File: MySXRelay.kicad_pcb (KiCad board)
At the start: 2 copper layers, 47.2 x 45.1 mm, 53 parts, among them K1 FH44L-1AT-L1-DC5V, Q1 2N7002, U1 MIC4427, U2 BL0942, U3 BP2525X, U4 Si8642BB-B-IS1, U5 MCP1703Ax-180xxTT

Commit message: update schematic to new version
- include MCU, remove MySXMotherboard
- only RS485 interface is isolated
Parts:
- removed X4: ~, Connector_PinSocket_2.54mm:PinSocket_1x04_P2.54mm_Vertical
- removed X5: ~, MySXRelay:JST-XH_S_4P-2.54MM-PIN1-RIGHT
- added C15: 100n, Capacitor_SMD:C_0402_1005Metric, F.Cu at (201.2, 95.6)
- added C16: 100n, Capacitor_SMD:C_0402_1005Metric, F.Cu at (201.2, 97.6)
- added C17: 100n, Capacitor_SMD:C_0402_1005Metric, F.Cu at (201.2, 99.5)
- added C18: 1u/50V, Capacitor_SMD:C_0603_1608Metric, F.Cu at (215.2, 102.4)
- added C19: 10u, Capacitor_SMD:C_0603_1608Metric, F.Cu at (215.2, 104.9)
- added D10: SMAJ11CA, Diode_SMD:D_SMA, F.Cu at (209.2, 101.4)
- added D8: LED, LED_SMD:LED_0805_2012Metric_Pad1.15x1.40mm_HandSolder, F.Cu at (185.9, 114.3)
- added D9: SMAJ11CA, Diode_SMD:D_SMA, F.Cu at (209.2, 96.9)
- added F1: Polyfuse, Fuse:Fuse_1206_3216Metric_Pad1.42x1.75mm_HandSolder, F.Cu at (208.1, 105.3)
- added F2: Polyfuse, Fuse:Fuse_1206_3216Metric_Pad1.42x1.75mm_HandSolder, F.Cu at (208.1, 108.6)
- added J1: AVR ISP, Connector_PinHeader_2.54mm:PinHeader_2x03_P2.54mm_Vertical, F.Cu at (194.3, 108.6)
- added J2: PRG/BL0942, Connector_PinHeader_2.54mm:PinHeader_1x02_P2.54mm_Vertical, F.Cu at (197.5, 96.9)
- added Q2: ~, Package_TO_SOT_SMD:SOT-23, F.Cu at (219.7, 108.2)
- added R19: 1k, Resistor_SMD:R_0603_1608Metric, F.Cu at (201.1, 107.5)
- added R20: 1M, Resistor_SMD:R_0603_1608Metric, F.Cu at (201.1, 110.0)
- added R21: 9.1k, Resistor_SMD:R_0603_1608Metric, F.Cu at (215.2, 107.5)
- added R22: 1M, Resistor_SMD:R_0603_1608Metric, F.Cu at (201.1, 112.5)
- added R23: 3k, Resistor_SMD:R_0603_1608Metric, F.Cu at (215.2, 110.0)
- added U6: ATmega328PB-A, Package_QFP:TQFP-32_7x7mm_P0.8mm, F.Cu at (189.3, 100.4)
- added U7: AT25xxx, Package_SO:SOIC-8_3.9x4.9mm_P1.27mm, F.Cu at (187.7, 109.6)
- added U8: AP2204K-ADJ, Package_TO_SOT_SMD:SOT-23-5, F.Cu at (219.8, 103.6)
- added U9: ST485E, Package_SO:SOIC-8_3.9x4.9mm_P1.27mm, F.Cu at (217.5, 98.0)
- C4: value 10n/50V -> 100n/50V
- C6: value 470u/10V -> 1u/50V; footprint Capacitor_THT:CP_Radial_D8.0mm_P3.50mm -> Capacitor_SMD:C_0603_1608Metric
- C7: value 1u -> 470u/10V; footprint Capacitor_SMD:C_0603_1608Metric -> Capacitor_THT:CP_Radial_D8.0mm_P3.50mm
- R4: value 27 -> 10k
- R5: value 1k -> 27
- R6: value 10k -> 1k
- X1: footprint Connector_PinSocket_2.54mm:PinSocket_2x10_P2.54mm_Vertical -> MySXRelay:JST-XH_S_4P-2.54MM-PIN1-RIGHT
- moved X1 79.4 mm to (212.6, 125.7)
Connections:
- net SW renamed /MCU/SW
- C1 pad 1: VCC -> +5V
- C1 pad 2: GND -> N_IN
- C14 pad 1: VCC -> +5VD
- C14 pad 2: GND -> GND1
- C2 pad 1: VCC -> +5V
- C2 pad 2: GND -> N_IN
- C3 pad 2: GND -> N_IN
- C4 pad 1: D4_INT -> D3
- C4 pad 2: GND -> N_IN
- C6 pad 1: Net-(U5-VI) -> Net-(D7-K)
- C6 pad 2: N_IN -> Net-(D6-K)
- C7 pad 1: Net-(D7-K) -> +5V
- C7 pad 2: Net-(D6-K) -> N_IN
- D1 pad 1: GND -> N_IN
- D1 pad 2: VCC -> +5V
- D2 pad 1: GND -> N_IN
- D2 pad 2: VCC -> +5V
- D3 pad 1: GND -> N_IN
- D3 pad 2: VCC -> +3V3
- D3 pad 3: D4_INT -> D3
- D4 pad 1: VCC -> +3V3
- D4 pad 2: GND -> N_IN
- L1 pad 2: Net-(U5-VI) -> +5V
- Q1 pad 2: GND -> N_IN
- R2 pad 2: D4_INT -> D3
- R3 pad 1: D6_PWM -> D6
- R3 pad 2: GND -> N_IN
- R4 pad 1: D6_PWM -> D3
- R4 pad 2: Net-(Q1-G) -> N_IN
- R5 pad 1: LED -> D6
- R5 pad 2: Net-(Q1-D) -> Net-(Q1-G)
- R6 pad 1: D4_INT -> /MCU/LED
- R6 pad 2: GND -> Net-(Q1-D)
- R8 pad 2: Net-(U5-VI) -> +5V
- R9 pad 1: Net-(U5-VI) -> +5V
- U1 pad 2: D5_PWM -> D5
- U1 pad 3: GND -> N_IN
- U1 pad 6: VCC -> +5V
- U2 pad 10: TX -> BL0942_TX
- U2 pad 6: CF1 -> D2
- U2 pad 9: RX -> BL0942_RX
- U4 pad 11: GND -> GND1
- U4 pad 12: D11_MOSI_TX -> Net-(U4-B3)
- U4 pad 13: D12_MISO_RX -> Net-(U4-B2)
- U4 pad 14: D3_INT -> Net-(U4-B1)
- U4 pad 15: GND -> GND1
- U4 pad 16: VCC -> +5VD
- U4 pad 3: CF1 -> D9
- U4 pad 4: TX -> RS485_TX
- U4 pad 5: RX -> RS485_RX
- U4 pad 9: GND -> GND1
- U5 pad 3: Net-(U5-VI) -> +5V
- X1 pad 1: VRAW -> Net-(Q2-D)
- X1 pad 2: VCC -> Net-(X1-Pin_2)
- X1 pad 3: VCC -> Net-(X1-Pin_3)
- X1 pad 4: GND -> GND1
- X3 pad 1: LED -> /MCU/LED
- X3 pad 3: VCC -> +3V3
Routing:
- net (no net): track 0.00 -> 278.5 mm
- net GND: track 74.3 -> 0.00 mm, vias 4 -> 0
- net VCC: track 71.1 -> 0.00 mm, vias 3 -> 0
- net D5_PWM: track 31.7 -> 0.00 mm, vias 2 -> 0
- net D5: track 0.00 -> 31.7 mm, vias 0 -> 2
- net Net-(U4-B3): track 0.00 -> 29.1 mm, vias 0 -> 1
- net D11_MOSI_TX: track 29.1 -> 0.00 mm, vias 1 -> 0
- net Net-(U4-B2): track 0.00 -> 24.0 mm, vias 0 -> 1
- net D12_MISO_RX: track 24.0 -> 0.00 mm, vias 1 -> 0
- net Net-(X4-Pin_4): track 18.9 -> 0.00 mm
- net Net-(U4-B1): track 0.00 -> 17.6 mm, vias 0 -> 1
- net D3_INT: track 17.6 -> 0.00 mm, vias 1 -> 0
- net Net-(X4-Pin_3): track 17.4 -> 0.00 mm
- net Net-(U5-VI): track 16.3 -> 0.00 mm
- net LED: track 15.3 -> 0.00 mm
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- added copper zone on F.Cu, net GND1
- added copper zone on B.Cu, net Net-(Q1-D)
- removed copper zone on B.Cu, net GND
- removed copper zone on F.Cu, net GND

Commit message: update pcb (WIP)
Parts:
- removed C2: 1u, Capacitor_SMD:C_0603_1608Metric
- removed C3: 22u, Capacitor_SMD:C_1206_3216Metric
- removed D1, D2: BAT54S, Package_TO_SOT_SMD:SOT-23
- removed K1: FH44L-1AT-L1-DC5V, MySXRelay:RELAY-TH_FH44L-1AT-L1-DC5V
- removed R1: 10k, Resistor_SMD:R_0603_1608Metric
- removed R21: 9.1k, Resistor_SMD:R_0603_1608Metric
- removed R23: 3k, Resistor_SMD:R_0603_1608Metric
- removed U1: MIC4427, Package_SO:SOIC-8_3.9x4.9mm_P1.27mm
- added J3: Relay, MySXRelay:edge_connector, F.Cu at (175.8, 110.5)
- C1: value 100n -> 10u; footprint Capacitor_SMD:C_0402_1005Metric -> Capacitor_SMD:C_0603_1608Metric; moved to F.Cu
- C10, C11, C13, C14, C8, C9, D4, D6, D7, R10, R11, R7, R8, R9, U2, U3, U4, U5: moved to F.Cu
- C16, D9, F1, F2, J1, J2, R20, U7: moved to B.Cu
- moved U9 69.6 mm to (150.3, 116.4), turned to 180 degrees
- moved U8 59.9 mm to (160.8, 113.5), turned to 90 degrees
- moved F1 59.2 mm to (149.2, 110.5)
- moved C18 59.0 mm to (157.5, 114.8), turned to 180 degrees
- moved Q2 57.3 mm to (163.1, 117.4)
- moved C19 56.8 mm to (158.7, 110.1), turned to 180 degrees
- moved X1 54.8 mm to (159.4, 112.7), turned to -90 degrees
- moved F2 54.2 mm to (154.0, 110.5), turned to 180 degrees
- moved D10 54.0 mm to (157.6, 117.3), turned to 180 degrees
- moved R20 53.7 mm to (148.2, 100.5), turned to -90 degrees
- moved C16 53.3 mm to (147.9, 98.3)
- moved R22 52.7 mm to (153.7, 89.6), turned to 180 degrees
- moved D9 51.0 mm to (161.5, 114.8), turned to -90 degrees
- moved J1 50.1 mm to (150.6, 84.0), turned to 180 degrees
- moved J2 45.9 mm to (153.4, 84.0), turned to 180 degrees
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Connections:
- C1 pad 1: +5V -> GND1
- C1 pad 2: N_IN -> Net-(U8-ADJ)
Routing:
- net (no net): track 278.5 -> 0.00 mm
- net MISO: track 0.00 -> 45.3 mm, vias 0 -> 4
- net D2: track 0.00 -> 45.0 mm, vias 0 -> 2
- net GND1: track 0.00 -> 43.8 mm, vias 4 -> 2
- net BL0942_RX: track 0.00 -> 42.4 mm, vias 0 -> 4
- net +3V3: track 69.3 -> 98.9 mm
- net Net-(D1-COM): track 29.2 -> 0.00 mm, vias 2 -> 0
- net +5V: track 0.00 -> 25.2 mm, vias 0 -> 1
- net SCK: track 0.00 -> 23.8 mm, vias 0 -> 3
- net BL0942_TX: track 0.00 -> 23.2 mm, vias 0 -> 1
- net Net-(D9-A2): track 0.00 -> 22.3 mm, vias 0 -> 1
- net /MCU/LED: track 0.00 -> 22.1 mm, vias 0 -> 1
- net +5VD: track 0.00 -> 20.8 mm, vias 0 -> 4
- net /MCU/A1: track 0.00 -> 20.5 mm, vias 0 -> 2
- net Net-(U4-B2): track 24.0 -> 4.31 mm, vias 1 -> 0
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- added copper zone on F.Cu, net Net-(D5-K)
- removed copper zone on F.Cu, net GND1
- removed copper zone on B.Cu, net N_IN
- removed copper zone on F.Cu, net N_IN
- removed copper zone on B.Cu, net Net-(D5-K)
- removed copper zone on B.Cu, net Net-(Q1-D)
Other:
- board size 47.2 x 45.1 mm -> 36 x 36.6 mm

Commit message: update pcb (WIP)
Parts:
- C1: value 10u -> 100p; footprint Capacitor_SMD:C_0603_1608Metric -> Capacitor_SMD:C_0402_1005Metric
- moved C1 9.10 mm to (161.0, 110.9)
- moved D4 1.03 mm to (167.7, 107.3)
- moved D8 0.98 mm to (166.8, 105.2)
- moved R19 0.70 mm to (166.9, 103.5)
- moved D9 0.65 mm to (161.5, 115.5)
- moved C19 0.38 mm to (158.3, 110.1)
- moved U4 0.33 mm to (151.6, 107.9)
- moved C18 0.30 mm to (157.2, 114.8)
- moved C14 0.30 mm to (157.8, 111.3)
- moved F1 0.23 mm to (149.0, 110.4)
- moved F2 0.12 mm to (154.0, 110.4)
- moved U8 0.05 mm to (160.7, 113.5)
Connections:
- net Net-(D5-K) renamed /BP2525_DRAIN
- net Net-(R17-Pad1) renamed L_SENSE
- net Net-(U3-CS) renamed /BP2525_CS
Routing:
- net Net-(U4-B1): track 1.27 -> 10.6 mm, vias 0 -> 2
- net +3V3: track 98.9 -> 106.5 mm, vias 5 -> 6
- net Net-(D10-A2): track 15.2 -> 20.0 mm, vias 2 -> 3
- net Net-(Q2-S): track 11.3 -> 14.6 mm
- net +5VD: track 20.8 -> 23.5 mm
- net GND1: track 43.8 -> 41.5 mm, vias 2 -> 3
- net D5: track 29.5 -> 31.6 mm
- net Net-(U8-ADJ): track 0.00 -> 1.50 mm, vias 1 -> 0
- net /MCU/LED: track 22.1 -> 23.1 mm
- net /MCU/A1: track 20.5 -> 19.7 mm
- net /MCU/SW: track 28.7 -> 29.6 mm
- net Net-(Q2-D): track 9.76 -> 10.1 mm, vias 1 -> 2

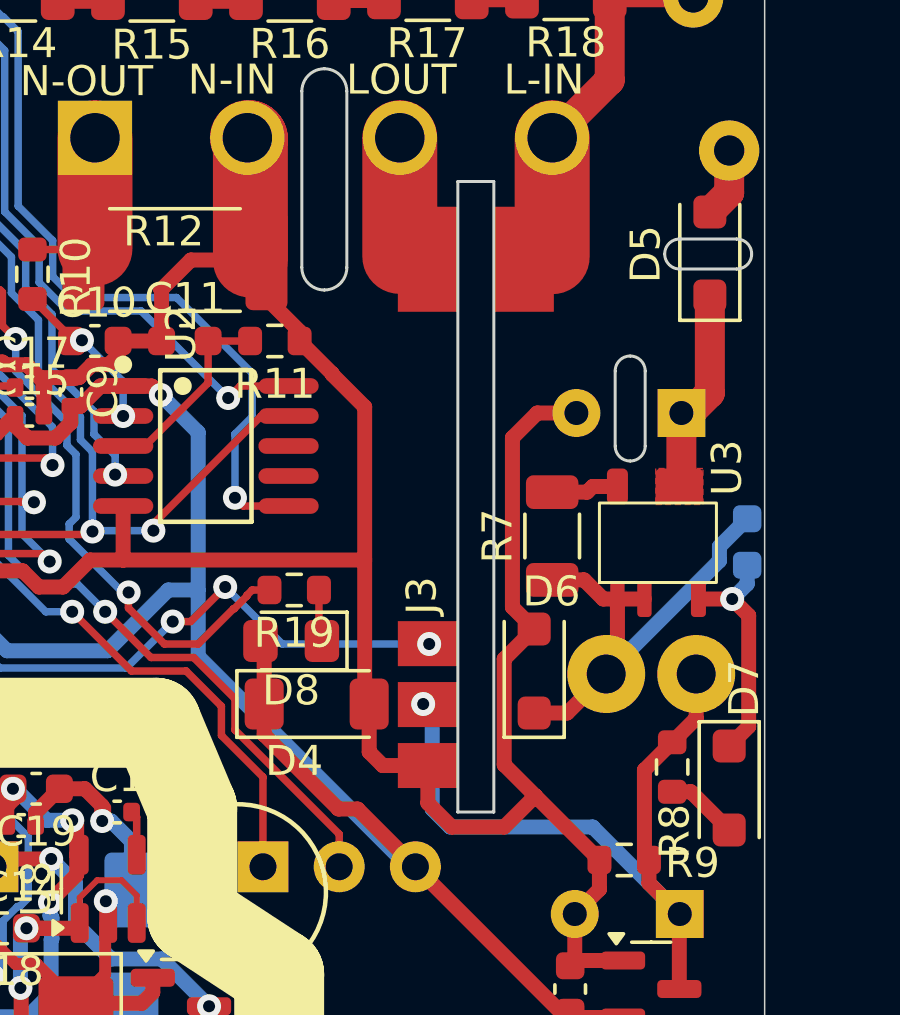
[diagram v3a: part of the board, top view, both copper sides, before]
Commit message: relay module updated
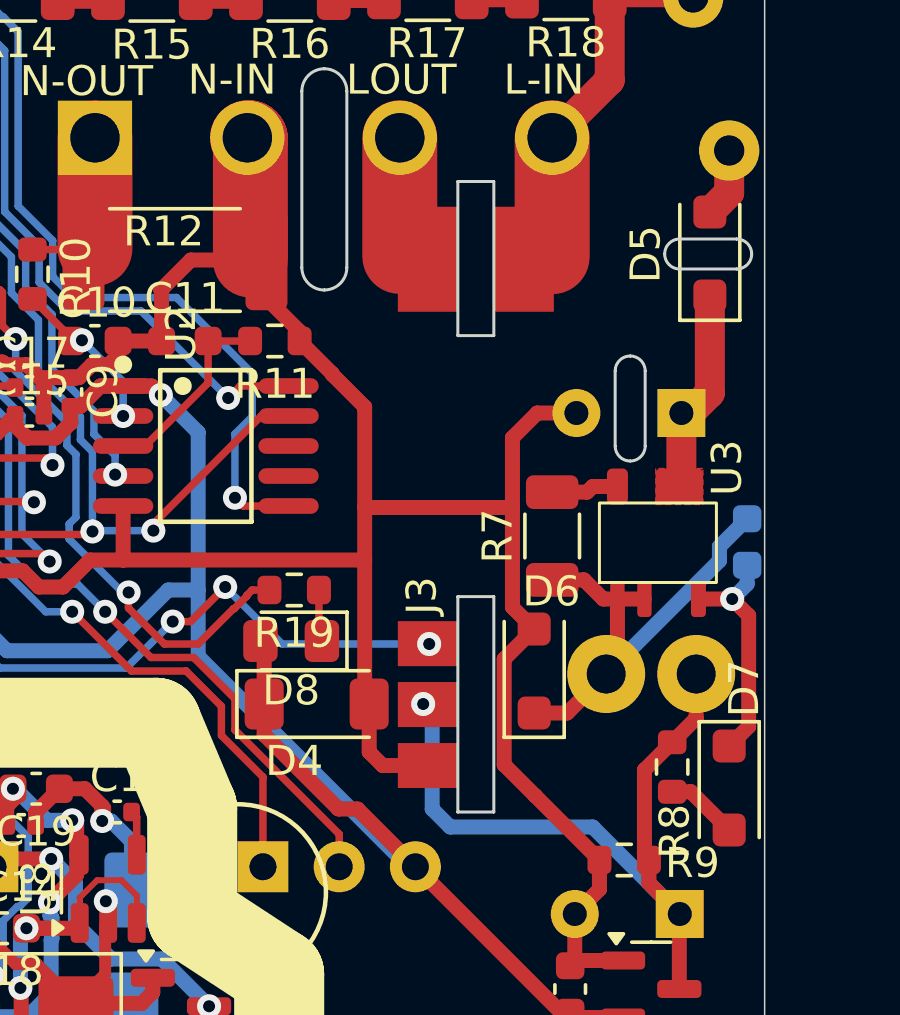
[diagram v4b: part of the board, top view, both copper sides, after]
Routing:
- net N_IN: track 132.0 -> 131.3 mm
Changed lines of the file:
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@@
 		(fp_line
 			(start 20.6364 -3.47)
-			(end -0.3816 -3.47)
+			(end 15.5 -3.47)
 			(stroke
 				(width 0.1)
@@
 		)
 		(fp_line
+			(start 15.5 -3.47)
+			(end 15.5 -2.27)
+			(stroke
+				(width 0.1)
+				(type default)
+			)
+			(layer "Edge.Cuts")
+		)
+		(fp_line
+			(start 6.8 -3.47)
+			(end -0.3816 -3.47)
+			(stroke
+				(width 0.1)
+				(type solid)
+			)
+			(layer "Edge.Cuts")
+		)
+		(fp_line
+			(start 6.8 -3.47)
+			(end 6.8 -2.27)
+			(stroke
+				(width 0.1)
+				(type default)
+			)
+			(layer "Edge.Cuts")
+		)
+		(fp_line
 			(start -0.3816 -3.47)
 			(end -0.3816 -2.27)
@@
 		(fp_line
 			(start 20.6364 -2.27)
+			(end 15.5 -2.27)
+			(stroke
+				(width 0.1)
+				(type solid)
+			)
+			(layer "Edge.Cuts")
+		)
+		(fp_line
+			(start 6.8 -2.27)
 			(end -0.3816 -2.27)
 			(stroke
@@
 		(fp_line
 			(start 16.2184 -3.6)
-			(end 6.0706 -3.6)
+			(end 16.2184 -5.5028)
 			(stroke
 				(width 0.05)
@@
 		)
 		(fp_line
-			(start 6.0706 -3.6)
-			(end 6.0706 -5.5214)
+			(start 16.2184 -3.6)
+			(end 6.0706 -3.6)
 			(stroke
 				(width 0.05)
@@
 		)
 		(fp_line
-			(start 0.3436 -3.6)
-			(end 0.3436 -5.5214)
+			(start 6.0706 -3.6)
+			(end 6.0706 -5.5214)
 			(stroke
 				(width 0.05)
@@
 		)
 		(fp_line
-			(start -0.5334 -3.6)
-			(end 0.3436 -3.6)
+			(start 0.3436 -3.6)
+			(end 0.3436 -5.5214)
 			(stroke
 				(width 0.05)
@@
 		)
 		(fp_line
-			(start 16.2184 -3.5814)
-			(end 16.2184 -5.5028)
+			(start -0.5334 -3.6)
+			(end 0.3436 -3.6)
 			(stroke
 				(width 0.05)
@@
 		(tags "capacitor")
 		(property "Reference" "C1"
-			(at 0 -1.16 360)
+			(at 0 -1.16 0)
 			(layer "F.SilkS")
 			(effects
@@
 		)
 		(property "Value" "100p"
-			(at 0 1.16 360)
+			(at 0 1.16 0)
 			(layer "F.Fab")
 			(effects
@@
 		)
 		(fp_text user "${REFERENCE}"
-			(at 0 0 360)
+			(at 0 0 0)
 			(layer "F.Fab")
 			(effects
@@
 	)
 	(segment
+		(start 174.175 100.75)
+		(end 169.275 100.75)
+		(width 0.5)
+		(layer "F.Cu")
+		(net 8)
+	)
+	(segment
 		(start 148.949666 96.924666)
 		(end 148.949666 98.595059)
@@
 	)
 	(segment
-		(start 173.9 111.4)
-		(end 174.9375 110.3625)
-		(width 0.5)
-		(layer "F.Cu")
-		(net 8)
-	)
-	(segment
 		(start 171.355 109.351)
 		(end 169.851 109.351)
@@
 	)
 	(segment
+		(start 174.175 98.425)
+		(end 174.175 100.75)
+		(width 0.5)
+		(layer "F.Cu")
+		(net 8)
+	)
+	(segment
 		(start 155.32 103.7)
 		(end 155.32 103.390001)
@@
 	)
 	(segment
-		(start 172.154 111.4)
-		(end 173.9 111.4)
-		(width 0.5)
-		(layer "F.Cu")
-		(net 8)
-	)
-	(segment
 		(start 169.4 108.9)
 		(end 169.4 107.3)
@@
 	)
 	(segment
+		(start 169.275 100.75)
+		(end 169.25 100.725)
+		(width 0.5)
+		(layer "F.Cu")
+		(net 8)
+	)
+	(segment
 		(start 168.168425 96.313425)
 		(end 169.25 97.395)
@@
 	)
 	(segment
+		(start 174.175 100.75)
+		(end 174.175 104.075)
+		(width 0.5)
+		(layer "F.Cu")
+		(net 8)
+	)
+	(segment
 		(start 159.455 96.42)
 		(end 159.726449 96.42)
@@
 	)
 	(segment
-		(start 169.25 97.395)
-		(end 169.25 107.15)
-		(width 0.5)
-		(layer "F.Cu")
-		(net 8)
-	)
-	(segment
 		(start 177.8625 115.85)
 		(end 176.275 115.85)
@@
 	)
 	(segment
-		(start 174.175 98.425)
-		(end 174.175 104.075)
-		(width 0.5)
-		(layer "F.Cu")
-		(net 8)
-	)
-	(segment
 		(start 174.9375 110.3625)
 		(end 177.075 112.5)
@@
 	)
 	(segment
+		(start 169.25 100.725)
+		(end 169.25 107.15)
+		(width 0.5)
+		(layer "F.Cu")
+		(net 8)
+	)
+	(segment
 		(start 158.555 96.561734)
 		(end 158.413266 96.42)
@@
 	)
 	(segment
-		(start 171.355 109.351)
-		(end 171.355 110.601)
-		(width 0.5)
-		(layer "F.Cu")
-		(net 8)
-	)
-	(segment
 		(start 167.08 94.88)
 		(end 167.08 95.2)
@@
 	)
 	(segment
-		(start 171.355 110.601)
-		(end 172.154 111.4)
+		(start 169.25 97.395)
+		(end 169.25 100.725)
 		(width 0.5)
 		(layer "F.Cu")

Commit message: finished PCB
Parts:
- moved R19 0.15 mm to (166.9, 103.3)
- moved D8 0.10 mm to (166.8, 105.1)
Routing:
- added copper zone on B.Cu, net GND1
- added copper zone on F.Cu, net GND1
- added copper zone on B.Cu, net N_IN
- added copper zone on F.Cu, net N_IN
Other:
- board text added: "+"
- board text added: "-"
- board text added: "MySXRelay v2.0"
- board text added: "SAFE"
- board text added: "SAFE VOLTAGE"
- board text added: "VOLTAGE"
- board text removed: "GND"
- board text removed: "MySXRelay v1.0"
- board text removed: "VIN"

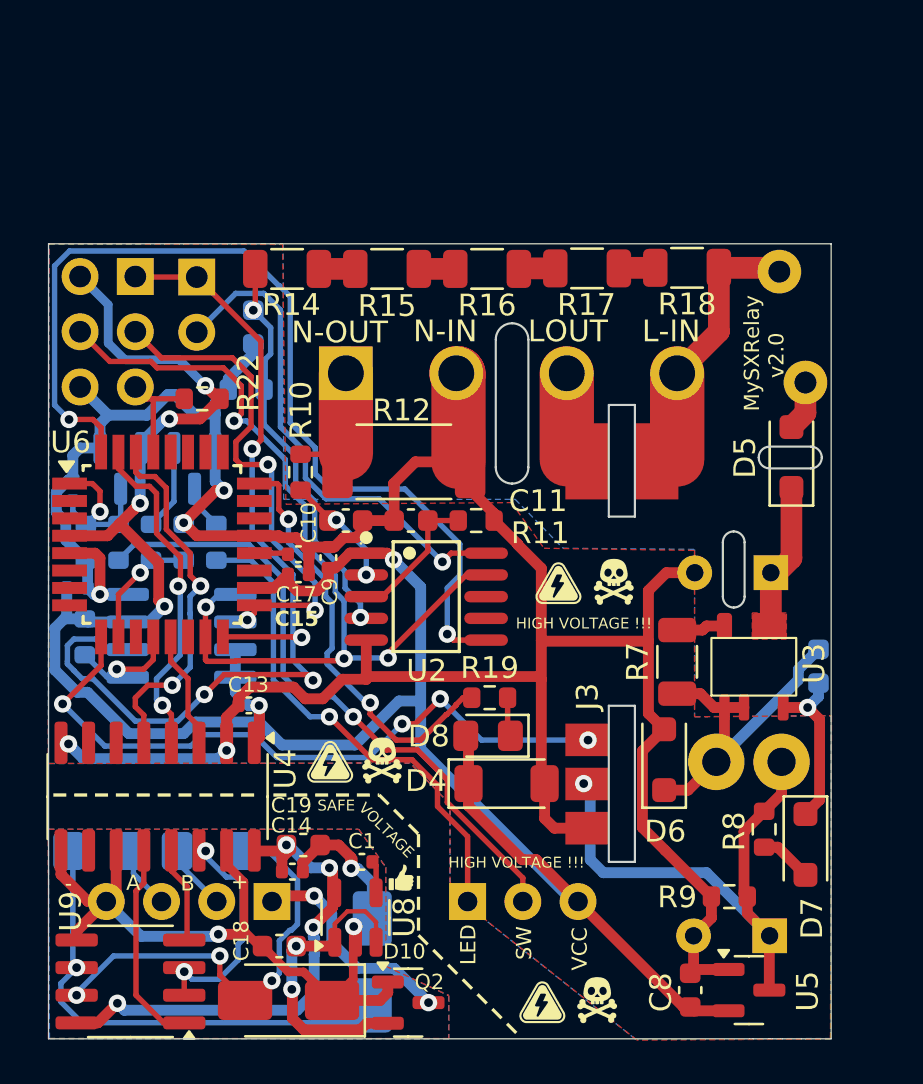
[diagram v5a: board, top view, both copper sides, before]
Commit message: changed mains connector
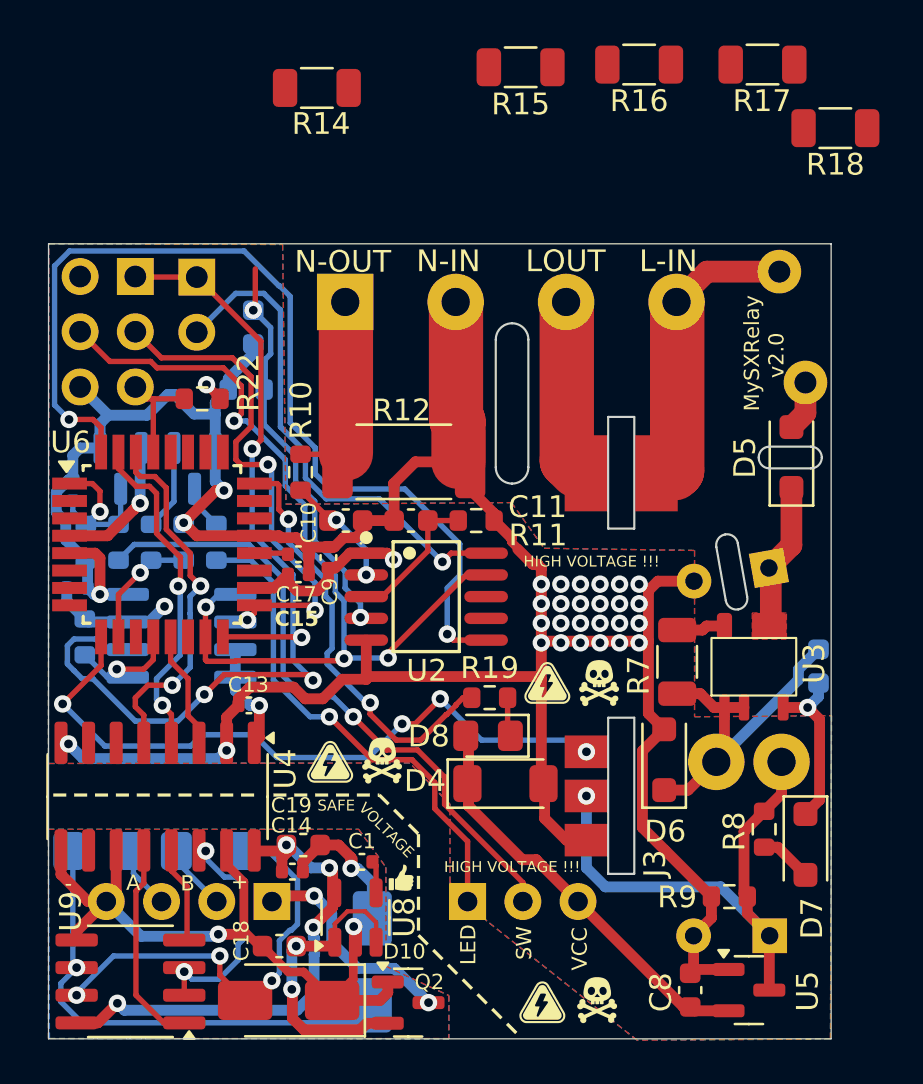
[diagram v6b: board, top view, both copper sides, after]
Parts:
- X2: footprint MySXRelay:MSTB_2,5_4-G -> TerminalBlock_Phoenix:TerminalBlock_Phoenix_MKDS-1,5-4-5.08_1x04_P5.08mm_Horizontal
- moved R17 12.4 mm to (179.4, 74.2)
- moved R16 11.7 mm to (173.8, 74.2)
- moved R15 11.1 mm to (168.3, 74.3)
- moved R18 9.37 mm to (182.8, 77.2)
- moved R14 8.44 mm to (158.9, 75.3)
- moved X2 3.28 mm to (160.2, 85.1), turned to 0 degrees
- moved J3 0.55 mm to (175.8, 111.1)
- moved C5 0.24 mm to (179.7, 97.4), turned to -170 degrees
- moved D4 0.05 mm to (167.6, 107.3)
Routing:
- net L_OUT: track 4.96 -> 8.46 mm
- net N_IN: track 131.4 -> 134.8 mm, vias 5 -> 29
- net N_OUT: track 5.53 -> 8.83 mm
- net +3V3: track 106.6 -> 104.4 mm, vias 6 -> 5
- net Net-(R16-Pad1): track 1.69 -> 0.00 mm
- net L_SENSE: track 1.69 -> 0.00 mm
- net Net-(R15-Pad1): track 1.67 -> 0.00 mm
- net Net-(R14-Pad1): track 1.67 -> 0.00 mm
- added copper zone on In2.Cu, net +3V3
- added copper zone on In1.Cu, net N_IN
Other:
- outline, holes or cut-outs redrawn
- copper layers 2 -> 4
